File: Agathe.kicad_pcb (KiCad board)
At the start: 2 copper layers, 338.8 x 114.8 mm, 173 parts, among them J1 Conn_01x04_Female, J2 Conn_01x02_Female, J4 Conn_01x02_Female, SW1 SW_Push, U1 ATmega32U4-AU, U2 PRTR5V0U2X, Y1 16MHz

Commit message: reverse vcc and gnd on leds (#9)
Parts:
- moved G*** 17.6 mm to (99.3, 155.8)
- moved MX59 12.1 mm to (362.2, 137.0)
- moved D21 12.1 mm to (181.8, 114.4)
- moved D63 12.1 mm to (130.3, 160.9)
- moved MX48 12.1 mm to (124.9, 138.5)
- moved MX4 12.1 mm to (132.1, 81.6)
- moved D52 12.1 mm to (222.3, 151.4)
- moved MX25 12.1 mm to (266.7, 100.3)
- moved MX50 12.1 mm to (162.1, 146.4)
- moved D24 12.1 mm to (256.3, 105.2)
- moved D65 12.1 mm to (160.6, 167.3)
- moved J1 12.1 mm to (175.8, 71.0)
- moved MX68 12.1 mm to (234.4, 165.6)
- moved MX47 12.1 mm to (104.4, 137.0)
- moved C2 12.1 mm to (201.2, 123.0)
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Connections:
- LED1 pad 1: GND -> +5V
- LED1 pad 3: +5V -> GND
- LED10 pad 1: GND -> +5V
- LED10 pad 3: +5V -> GND
- LED11 pad 1: GND -> +5V
- LED11 pad 3: +5V -> GND
- LED12 pad 1: GND -> +5V
- LED12 pad 3: +5V -> GND
- LED13 pad 1: GND -> +5V
- LED13 pad 3: +5V -> GND
- LED14 pad 1: GND -> +5V
- LED14 pad 3: +5V -> GND
- LED15 pad 1: GND -> +5V
- LED15 pad 3: +5V -> GND
- LED16 pad 1: GND -> +5V
- LED16 pad 3: +5V -> GND
- LED2 pad 1: GND -> +5V
- LED2 pad 3: +5V -> GND
- LED3 pad 1: GND -> +5V
- LED3 pad 3: +5V -> GND
- LED4 pad 1: GND -> +5V
- LED4 pad 3: +5V -> GND
- LED5 pad 1: GND -> +5V
- LED5 pad 3: +5V -> GND
- LED6 pad 1: GND -> +5V
- LED6 pad 3: +5V -> GND
- LED7 pad 1: GND -> +5V
- LED7 pad 3: +5V -> GND
- LED8 pad 1: GND -> +5V
- LED8 pad 3: +5V -> GND
- LED9 pad 1: GND -> +5V
- LED9 pad 3: +5V -> GND
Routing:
- net +5V: track 979.5 -> 1086.2 mm
- net GND: track 256.1 -> 264.2 mm, vias 9 -> 11

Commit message: add a capacitor
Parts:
- added C8: 0.1uF, Capacitor_SMD:C_0805_2012Metric, B.Cu at (199.6, 141.7)
- moved C5 9.63 mm to (206.5, 135.0), turned to 270 degrees
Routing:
- net +5V: track 1086.2 -> 1093.4 mm
- net GND: track 264.2 -> 270.3 mm
- net ROTA: track 255.0 -> 255.8 mm

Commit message: j'ai putain de tout refait putain
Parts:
- removed J2, J4: Conn_01x02_Female, Connector_PinHeader_2.54mm:PinHeader_1x02_P2.54mm_Vertical
- added J3: AVR-ISP-6, random-keyboard-parts:Reset_Pretty-Mask, B.Cu at (167.7, 121.5)
- U2: footprint Package_TO_SOT_SMD:SOT-143 -> random-keyboard-parts:SOT143B
- moved R1 62.6 mm to (175.5, 188.5), turned to 0 degrees
- moved C3 56.3 mm to (170.7, 175.2), turned to 180 degrees
- moved F1 53.1 mm to (175.8, 131.8)
- moved C2 53.0 mm to (191.9, 175.2), turned to 0 degrees
- moved R6 51.2 mm to (186.2, 126.1), turned to 180 degrees
- moved U2 51.1 mm to (181.1, 129.7)
- moved R5 51.1 mm to (176.4, 126.2), turned to 0 degrees
- moved J1 50.9 mm to (158.8, 118.9)
- moved C4 49.9 mm to (170.7, 184.5), turned to 90 degrees
- moved D73 49.9 mm to (335.7, 205.1)
- moved D56 49.9 mm to (283.3, 187.1)
- moved MX23 49.9 mm to (214.1, 155.6)
- moved MX36 49.9 mm to (160.1, 177.2)
- moved D74 49.9 mm to (354.7, 205.1)
- moved MX7 49.9 mm to (172.6, 140.9)
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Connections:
- net Net-(R4-Pad2) renamed RST
- J1 pad 2: D+ -> DP
- J1 pad 3: D- -> DN
- MX15 pad A: ROTA -> MISO
- MX30 pad A: ROTA -> MISO
- MX45 pad A: ROTA -> MISO
- R2 pad 1: Net-(R2-Pad1) -> D-
- R2 pad 2: D- -> DN
- R3 pad 1: Net-(R3-Pad1) -> D+
- R3 pad 2: D+ -> DP
- U1 pad 1: GPIO1 -> ROW0
- U1 pad 10: COL9 -> MOSI
- U1 pad 11: COL10 -> MISO
- U1 pad 12: COL11 -> ROTB
- U1 pad 18: COL13 -> COL6
- U1 pad 19: COL12 -> COL7
- U1 pad 20: ROW4 -> COL8
- U1 pad 21: ROW3 -> COL9
- U1 pad 22: ROW2 -> COL10
- U1 pad 25: COL5 -> COL11
- U1 pad 26: COL4 -> COL12
- U1 pad 27: COL3 -> COL13
- U1 pad 28: COL2 -> COL14
- U1 pad 29: COL1 -> COL0
- U1 pad 3: Net-(R2-Pad1) -> D-
- U1 pad 30: LED -> COL1
- U1 pad 31: COL0 -> COL2
- U1 pad 32: COL14 -> COL3
- U1 pad 36: COL6 -> COL4
- U1 pad 37: GPIO2 -> COL5
- U1 pad 38: COL7 -> ROW4
- U1 pad 39: COL8 -> ROW3
- U1 pad 4: Net-(R3-Pad1) -> D+
- U1 pad 40: ROW1 -> ROW2
- U1 pad 41: ROW0 -> ROW1
- U1 pad 8: ROTB -> LED
- U1 pad 9: ROTA -> SCK
- U2 pad 2: D+ -> DP
- U2 pad 3: D- -> DN
- USB1 pad A6: D+ -> DP
- USB1 pad A7: D- -> DN
- USB1 pad B6: D+ -> DP
- USB1 pad B7: D- -> DN
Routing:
- net GND: track 270.3 -> 1294.9 mm, vias 11 -> 8
- net MISO: track 0.00 -> 292.1 mm, vias 0 -> 2
- net ROTA: track 255.8 -> 0.00 mm, vias 2 -> 0
- net +5V: track 1093.4 -> 986.0 mm, vias 5 -> 8
- net GPIO1: track 89.1 -> 0.00 mm, vias 4 -> 0
- net D-: track 93.1 -> 7.46 mm
- net DP: track 0.00 -> 83.6 mm, vias 0 -> 2
- net DN: track 0.00 -> 83.1 mm, vias 0 -> 2
- net GPIO2: track 79.9 -> 0.00 mm, vias 4 -> 0
- net MOSI: track 0.00 -> 78.7 mm, vias 0 -> 1
- net D+: track 85.0 -> 7.46 mm, vias 2 -> 0
- net SCK: track 0.00 -> 77.0 mm, vias 0 -> 1
- net LED: track 108.5 -> 60.3 mm, vias 4 -> 0
- net COL14: track 379.0 -> 342.9 mm
- net RST: track 73.5 -> 101.5 mm, vias 0 -> 1
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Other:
- board text removed: "GND"
- board text removed: "PE6"
- board text removed: "PF6"
- board text removed: "VCC"

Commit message: add some stuff after a review from @plut0nium
Some new feature from the @masterzen blog article
http://www.masterzen.fr/2020/10/20/designing-a-keyboard-part3/
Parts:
- added C10: 0.1uF, Capacitor_SMD:C_0805_2012Metric, B.Cu at (38.5, 192.3)
- added C11: 0.1uF, Capacitor_SMD:C_0805_2012Metric, B.Cu at (263.9, 212.3)
- added C9: 0.1uF, Capacitor_SMD:C_0805_2012Metric, B.Cu at (373.5, 140.1)
- added FB1: Ferrite_Bead_Small, Inductor_SMD:L_0805_2012Metric_Pad1.15x1.40mm_HandSolder, B.Cu at (172.7, 117.3)
- added R7: 350, Resistor_SMD:R_0805_2012Metric, B.Cu at (189.7, 131.0)
- moved J1 30.0 mm to (185.1, 133.5)
- moved USB1 4.75 mm to (181.1, 114.0)
- moved F1 2.72 mm to (173.8, 129.9)
- moved SW1 0.84 mm to (199.1, 119.4)
- turned LED10 to 0 degrees
- turned LED11 to 348 degrees
- turned LED12 to 0 degrees
- turned LED13 to 270 degrees
- turned LED14 to 270 degrees
- turned LED15 to 180 degrees
- turned LED16 to 180 degrees
- turned LED2 to 180 degrees
- turned LED3 to 180 degrees
- turned LED4 to 180 degrees
- turned LED5 to 90 degrees
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- renumbered LED8 to LED10, LED7 to LED11, LED6 to LED12, LED5 to LED13, LED4 to LED14, LED3 to LED15, LED2 to LED16, LED16 to LED2, LED15 to LED3, LED14 to LED4, LED13 to LED5, LED12 to LED6, LED11 to LED7, LED10 to LED8
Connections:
- J1 pad 1: VCC -> GND
- J1 pad 4: GND -> VCC
- LED1 pad 4: LED -> Net-(LED1-Pad4)
- LED10 pad 2: Net-(LED8-Pad2) -> Net-(LED10-Pad2)
- LED10 pad 4: Net-(LED7-Pad2) -> Net-(LED10-Pad4)
- LED11 pad 2: Net-(LED7-Pad2) -> Net-(LED11-Pad2)
- LED11 pad 4: Net-(LED6-Pad2) -> Net-(LED10-Pad2)
- LED12 pad 2: Net-(LED6-Pad2) -> Net-(LED12-Pad2)
- LED12 pad 4: Net-(LED5-Pad2) -> Net-(LED11-Pad2)
- LED13 pad 2: Net-(LED5-Pad2) -> Net-(LED13-Pad2)
- LED13 pad 4: Net-(LED4-Pad2) -> Net-(LED12-Pad2)
- LED14 pad 2: Net-(LED4-Pad2) -> Net-(LED14-Pad2)
- LED14 pad 4: Net-(LED3-Pad2) -> Net-(LED13-Pad2)
- LED15 pad 2: Net-(LED3-Pad2) -> Net-(LED15-Pad2)
- LED15 pad 4: Net-(LED2-Pad2) -> Net-(LED14-Pad2)
- LED16 pad 2: Net-(LED2-Pad2) -> Net-(LED16-Pad2)
- LED16 pad 4: Net-(LED1-Pad2) -> Net-(LED15-Pad2)
- LED2 pad 2: Net-(LED16-Pad2) -> Net-(LED2-Pad2)
- LED2 pad 4: Net-(LED15-Pad2) -> Net-(LED1-Pad2)
- LED3 pad 2: Net-(LED15-Pad2) -> Net-(LED3-Pad2)
- LED3 pad 4: Net-(LED14-Pad2) -> Net-(LED2-Pad2)
- LED4 pad 2: Net-(LED14-Pad2) -> Net-(LED4-Pad2)
- LED4 pad 4: Net-(LED13-Pad2) -> Net-(LED3-Pad2)
- LED5 pad 2: Net-(LED13-Pad2) -> Net-(LED5-Pad2)
- LED5 pad 4: Net-(LED12-Pad2) -> Net-(LED4-Pad2)
- LED6 pad 2: Net-(LED12-Pad2) -> Net-(LED6-Pad2)
- LED6 pad 4: Net-(LED11-Pad2) -> Net-(LED5-Pad2)
- LED7 pad 2: Net-(LED11-Pad2) -> Net-(LED7-Pad2)
- LED7 pad 4: Net-(LED10-Pad2) -> Net-(LED6-Pad2)
- LED8 pad 2: Net-(LED10-Pad2) -> Net-(LED8-Pad2)
- LED8 pad 4: Net-(LED10-Pad4) -> Net-(LED7-Pad2)
- USB1 pad S1: GND -> Earth
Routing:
- net GND: track 1294.9 -> 1052.5 mm, vias 8 -> 7
- net Net-(LED6-Pad2): track 60.2 -> 34.1 mm
- net Net-(LED11-Pad2): track 34.1 -> 60.2 mm
- net DN: track 83.1 -> 57.5 mm, vias 2 -> 0
- net DP: track 83.6 -> 59.2 mm, vias 2 -> 0
- net Net-(LED5-Pad2): track 50.9 -> 34.5 mm
- net Net-(LED12-Pad2): track 34.5 -> 50.9 mm
- net Net-(LED4-Pad2): track 34.5 -> 49.6 mm
- net Net-(LED13-Pad2): track 49.6 -> 34.5 mm
- net Net-(LED2-Pad2): track 65.2 -> 50.8 mm
- net Net-(LED15-Pad2): track 50.8 -> 65.2 mm
- net LED: track 60.3 -> 48.1 mm
- net Net-(LED1-Pad4): track 0.00 -> 11.0 mm
- net Net-(LED7-Pad2): track 46.7 -> 56.5 mm
- net Net-(LED10-Pad2): track 56.5 -> 46.7 mm
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- added copper zone on B.Cu, net Earth
- added copper zone on F.Cu, net Earth
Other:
- board size 338.8 x 114.8 mm -> 338.8 x 118.7 mm
- board text added: "BISOUS"

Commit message: add a breakable usb port and matrix encoder
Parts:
- added D44: D_Small, Diode_SMD:D_SOD-123, B.Cu at (351.0, 129.9)
- added D60: D_Small, Diode_SMD:D_SOD-123, B.Cu at (354.9, 149.0)
- added D62: D_Small, Diode_SMD:D_SOD-123, B.Cu at (358.9, 168.0)
- added FB2: Ferrite_Bead_Small, Inductor_SMD:L_0805_2012Metric_Pad1.15x1.40mm_HandSolder, B.Cu at (155.6, 108.6)
- added J2: Conn_01x04_Female, Connector_PinHeader_2.54mm:PinHeader_1x04_P2.54mm_Vertical, B.Cu at (152.9, 112.5)
- added R8: 5.1k, Resistor_SMD:R_0805_2012Metric, B.Cu at (142.4, 112.1)
- added R9: 5.1k, Resistor_SMD:R_0805_2012Metric, B.Cu at (142.4, 108.6)
- added REF**: Generic-Mounthole, random-keyboard-parts:Generic-Mounthole, F.Cu at (159.1, 103.6)
- added REF**: Generic-Mounthole, random-keyboard-parts:Generic-Mounthole, F.Cu at (159.1, 112.0)
- added REF**: Generic-Mounthole, random-keyboard-parts:Generic-Mounthole, F.Cu at (138.9, 112.0)
- added REF**: Generic-Mounthole, random-keyboard-parts:Generic-Mounthole, F.Cu at (138.9, 103.6)
- added REF**: breakaway-mousebites, random-keyboard-parts:breakaway-mousebites, F.Cu at (148.6, 115.2)
- added USB2: USB_C_Receptacle_USB2.0, Connector_USB:USB_C_Receptacle_HRO_TYPE-C-31-M-12, B.Cu at (149.0, 104.1)
- moved D15 2.00 mm to (347.5, 129.9)
- moved D30 2.00 mm to (351.4, 149.0)
- moved D45 2.00 mm to (355.4, 168.0)
- moved C11 0.18 mm to (263.9, 212.1)
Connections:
- MX15 pad C: GND -> Net-(D44-Pad2)
- MX30 pad C: GND -> Net-(D60-Pad2)
- MX45 pad C: GND -> Net-(D62-Pad2)
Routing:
- net GND: track 1052.5 -> 997.1 mm
- net Net-(FB2-Pad1): track 0.00 -> 25.3 mm, vias 0 -> 2
- net Net-(R8-Pad2): track 0.00 -> 17.4 mm
- net Net-(J2-Pad4): track 0.00 -> 11.5 mm, vias 0 -> 2
- net Net-(D62-Pad2): track 0.00 -> 8.41 mm
- net Net-(D60-Pad2): track 0.00 -> 8.30 mm
- net Net-(D44-Pad2): track 0.00 -> 8.12 mm
- net Net-(R9-Pad2): track 0.00 -> 7.79 mm
- net Net-(J2-Pad2): track 0.00 -> 7.77 mm
- net Net-(J2-Pad3): track 0.00 -> 6.59 mm
- net ETH: track 0.00 -> 2.40 mm
- net ROW0: track 323.7 -> 325.2 mm
- net ROW1: track 314.1 -> 315.6 mm
- net ROW2: track 321.7 -> 323.1 mm
- net Net-(D15-Pad2): track 18.9 -> 19.7 mm
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- added copper zone on B.Cu, net ETH
- added copper zone on F.Cu, net ETH
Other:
- board size 338.8 x 118.7 mm -> 338.8 x 129.1 mm

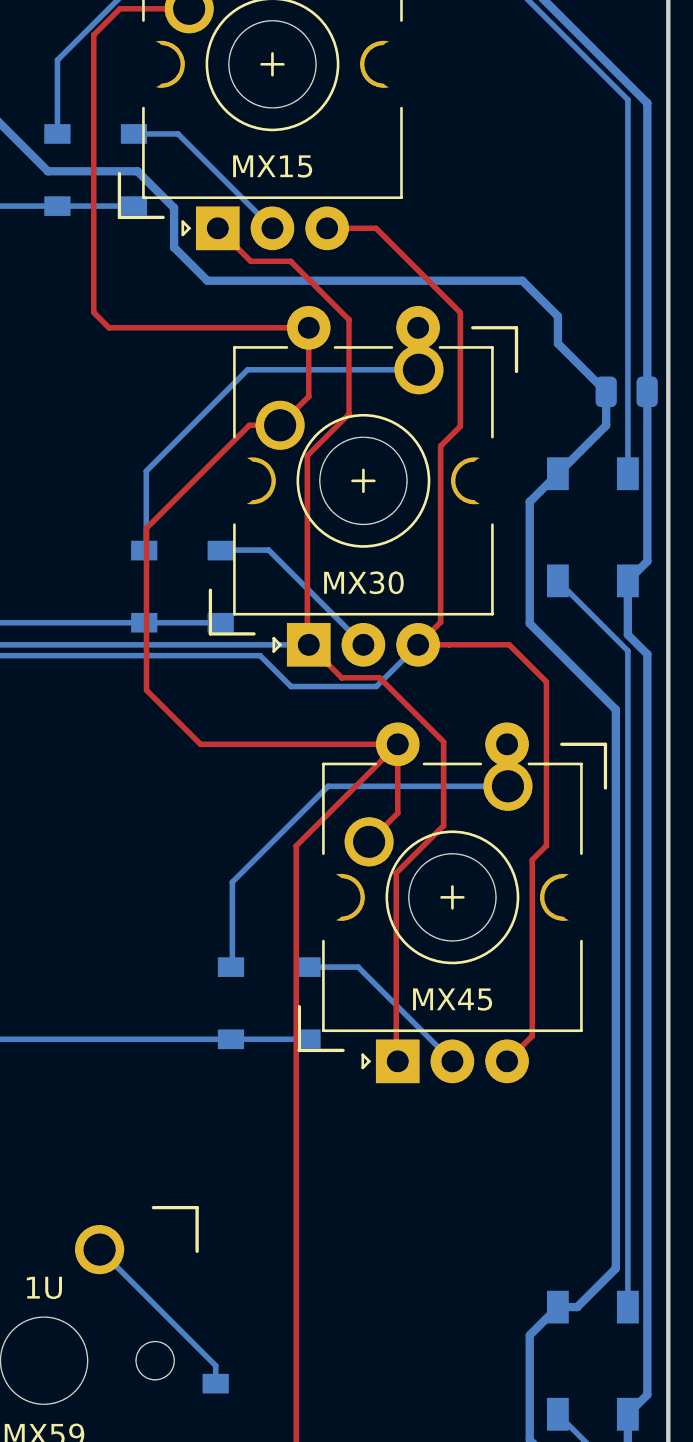
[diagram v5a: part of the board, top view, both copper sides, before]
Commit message: add matrice rotary possibilities
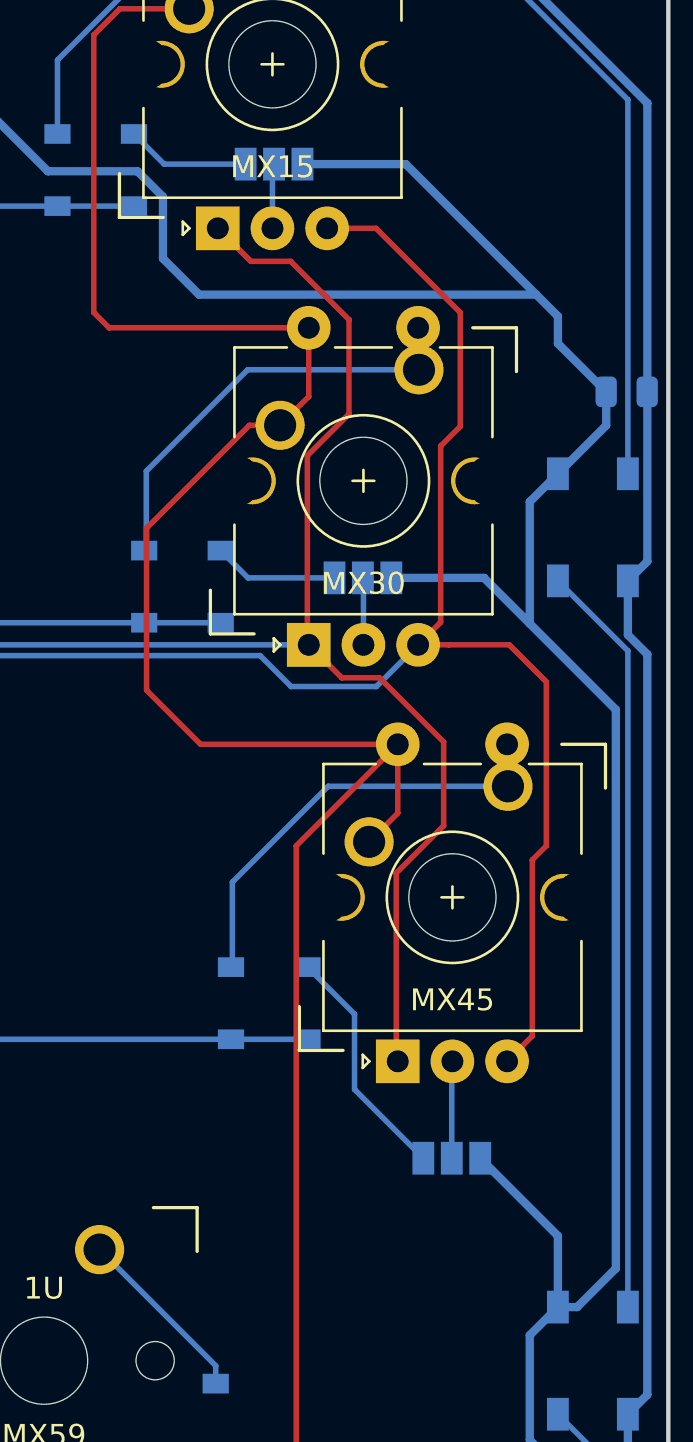
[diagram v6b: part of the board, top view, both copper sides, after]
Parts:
- added JP1: SolderJumper_3_Open, Jumper:SolderJumper-3_P1.3mm_Open_Pad1.0x1.5mm_NumberLabels, B.Cu at (357.4, 129.7)
- added JP2: SolderJumper_3_Open, Jumper:SolderJumper-3_P1.3mm_Open_Pad1.0x1.5mm_NumberLabels, B.Cu at (361.4, 148.6)
- added JP3: SolderJumper_3_Open, Jumper:SolderJumper-3_P1.3mm_Open_Pad1.0x1.5mm_NumberLabels, B.Cu at (365.5, 175.1)
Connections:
- MX15 pad C: Net-(D44-Pad2) -> Net-(JP1-Pad2)
- MX30 pad C: Net-(D60-Pad2) -> Net-(JP2-Pad2)
- MX45 pad C: Net-(D62-Pad2) -> Net-(JP3-Pad2)
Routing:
- net GND: track 997.1 -> 1026.3 mm
- net Net-(JP3-Pad2): track 0.00 -> 4.44 mm
- net Net-(JP2-Pad2): track 0.00 -> 3.07 mm
- net Net-(JP1-Pad2): track 0.00 -> 2.97 mm
- net Net-(D60-Pad2): track 8.30 -> 5.72 mm
- net Net-(D62-Pad2): track 8.41 -> 10.9 mm
- net Net-(D44-Pad2): track 8.12 -> 5.68 mm
